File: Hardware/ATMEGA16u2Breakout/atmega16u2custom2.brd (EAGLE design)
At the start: 61.9 x 45.7 mm, 59 parts, among them IC10 74LVC1G125DBV, J3 USB-MICRO B, U1 ATMEGA8U2AU

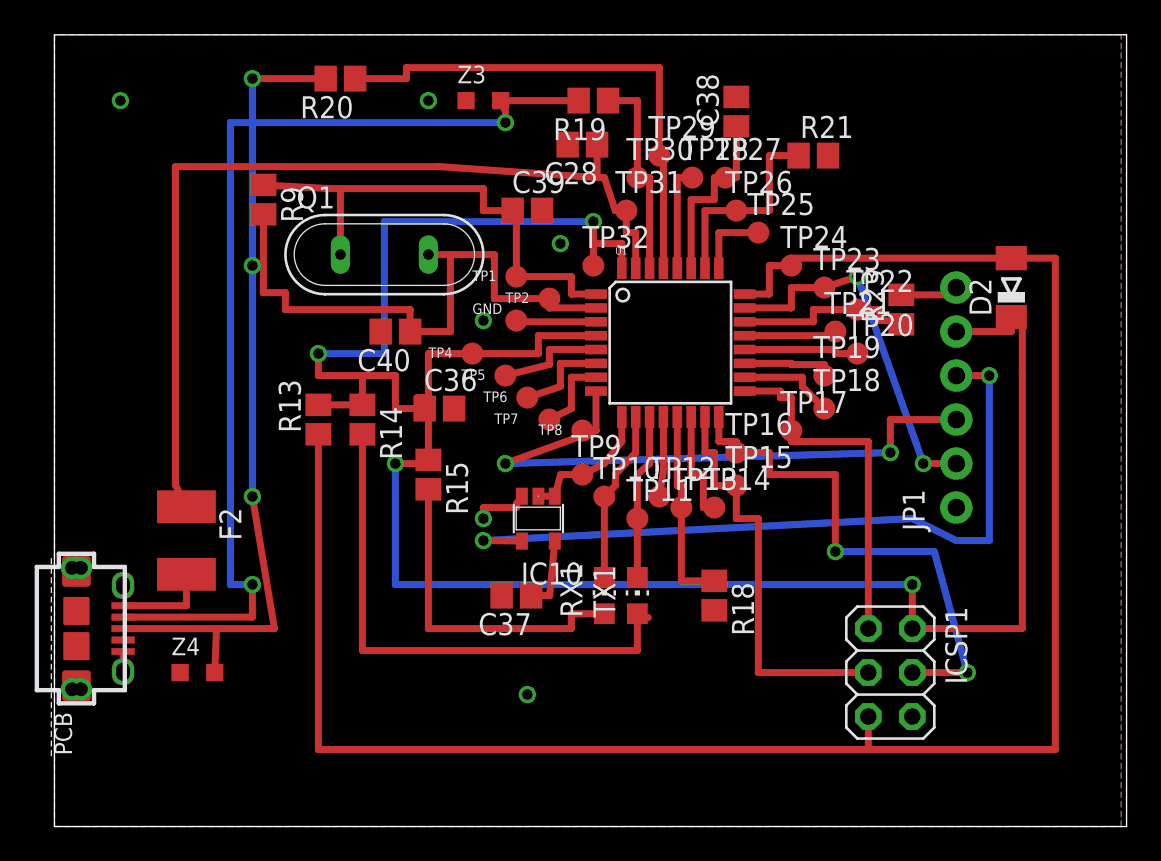
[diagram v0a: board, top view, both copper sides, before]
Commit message: ATMEGA16u2 Board Update
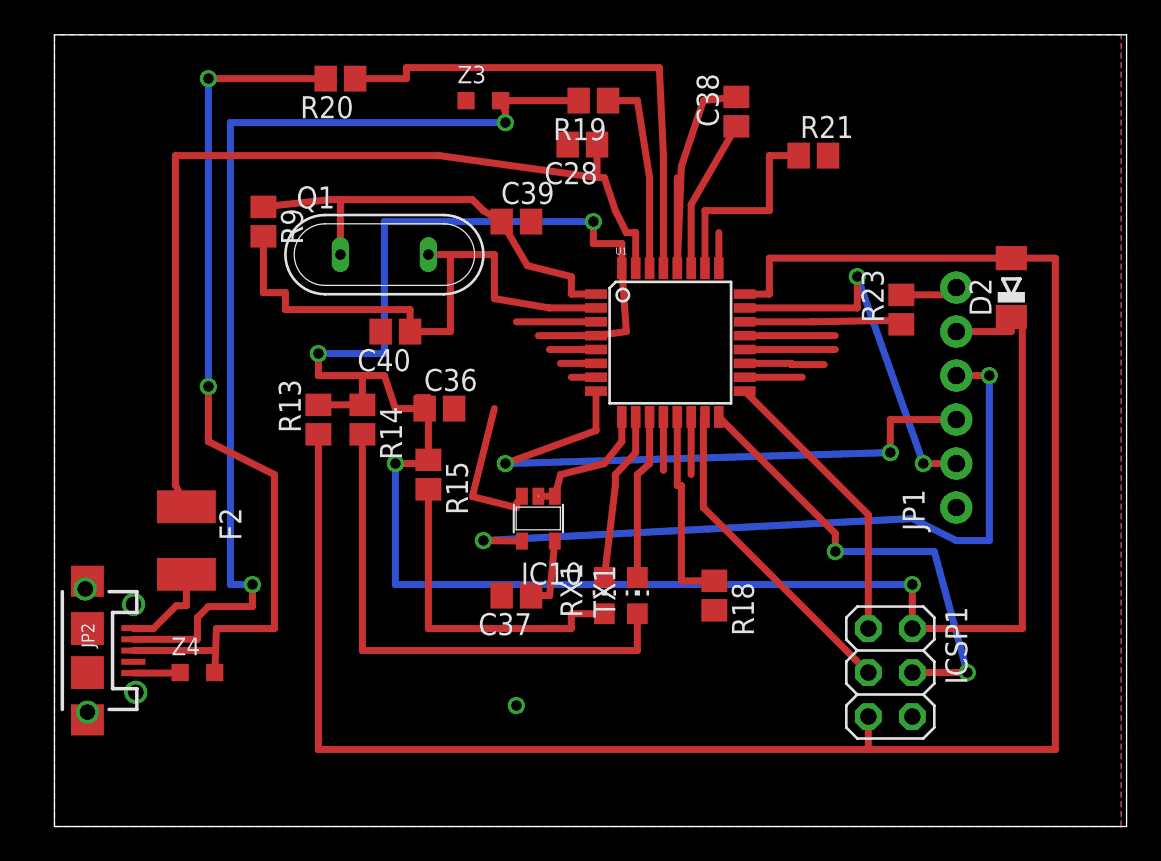
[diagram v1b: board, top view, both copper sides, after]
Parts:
- removed GND, TP1, TP10, TP11, TP12, TP13, TP14, TP15, TP16, TP17, TP18, TP19, TP2, TP20, TP21, TP22, TP23, TP24, TP25, TP26, TP27, TP28, TP29, TP30, TP31, TP32, TP4, TP5, TP6, TP7, TP8, TP9: TPB1,27, testpad:B1,27
- removed J3: USB-MICRO B, SmartPrj:CON2_USB_MICRO_B_AT
- added JP2: USB-MICROB, SparkFun-Connectors:USB-MICROB
- moved R9 1.27 mm to (12.1, 34.9)
- moved C39 0.90 mm to (26.7, 34.9)
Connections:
- net +5V: no longer TP32.TP, TP4.TP
- net 16U2-TX: no longer TP9.TP
- net 8PB4: no longer TP18.TP
- net 8PB5: no longer TP19.TP
- net 8PB6: no longer TP20.TP
- net BD+: now also JP2.D+; no longer J3.P3
- net BD-: now also JP2.D-; no longer J3.P2
- net DTR: no longer TP13.TP
- net ERASE_CMD: no longer TP23.TP
- net GND: now also JP2.GND, JP2.MT1, JP2.MT2; no longer GND.TP, J3.P$1, J3.P$2, J3.P$3, J3.P$4, J3.P$5, J3.P$6, J3.P$7, J3.P$8, J3.P5, J3.S1, J3.S2, J3.S3, J3.S4, J3.S5, J3.S6, TP28.TP
- net MISO2: no longer TP17.TP
- net MOSI2: no longer TP16.TP
- net N$1: no longer TP26.TP
- net N$2: no longer TP5.TP
- net N$3: no longer TP6.TP
- net N$5: no longer TP7.TP
- net N$6: no longer TP12.TP
- net N$7: no longer TP25.TP
- net N$8: no longer TP14.TP
- net N$9: no longer TP21.TP
- net RD+: no longer TP29.TP
- net RD-: no longer TP30.TP
- net RESET2: no longer TP24.TP
- net RESET_CMD: no longer TP22.TP
- net RXL-U2: no longer TP10.TP
- net SCK2: no longer TP15.TP
- net TX: no longer TP8.TP
- net TXL-U2: no longer TP11.TP
- net USBVCCU2: no longer TP31.TP
- net VUCAP: no longer TP27.TP
- net XT1: no longer TP1.TP
- net XT2: no longer TP2.TP
- net XVCC: now also JP2.VBUS; no longer J3.P1
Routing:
- net GND: track 15.1 -> 33.0 mm, vias 7 -> 5
- net +5V: track 131.4 -> 125.2 mm
- net SCK2: track 24.2 -> 18.7 mm
- net MISO2: track 20.8 -> 16.7 mm
- net BD+: track 47.4 -> 51.5 mm
- net MOSI2: track 30.6 -> 26.7 mm
- net XT1: track 29.1 -> 25.4 mm
- net N$2: track 6.18 -> 2.69 mm
- net N$3: track 5.41 -> 2.06 mm
- net N$8: track 6.57 -> 3.33 mm
- net N$5: track 4.65 -> 1.42 mm
- net 8PB4: track 5.66 -> 3.33 mm
- net N$7: track 4.34 -> 2.06 mm
- net VUCAP: track 10.8 -> 8.89 mm
- net XT2: track 34.8 -> 33.0 mm
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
